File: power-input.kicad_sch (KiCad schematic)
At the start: 21 parts, among them J204 Conn_01x02, J301 Conn_01x02, U202 XL1509-3.3

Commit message: Rename and update layout
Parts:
- removed C201: 22nF, Capacitor_SMD:C_0402_1005Metric, symbol Device:C_Small
- removed D201: B5819W, Diode_SMD:D_SOD-123, symbol Device:D_Schottky
- removed J204: Conn_01x02, Connector_PinHeader_2.54mm:PinHeader_1x02_P2.54mm_Vertical, symbol Connector_Generic:Conn_01x02
- removed J301: Conn_01x02, Connector_Phoenix_MC:PhoenixContact_MCV_1,5_2-G-3.81_1x02_P3.81mm_Vertical, symbol Connector_Generic:Conn_01x02
- removed R211: 0, Resistor_SMD:R_0402_1005Metric, symbol Device:R_Small
- removed R212: inf, Resistor_SMD:R_0402_1005Metric, symbol Device:R_Small
- added C606: 100nF/50V, Capacitor_SMD:C_0402_1005Metric, symbol Device:C
- FB601: renamed from FB301; symbol Device:Ferrite_Bead -> Device:FerriteBead
- renumbered C306 to C601, C302 to C602, C307 to C603, C308 to C604, C301 to C605, C304 to C607, D301 to D601, D303 to D602, D302 to D603, F301 to F601, L302 to L601, L301 to L602, R304 to R601, U202 to U601
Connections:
- net FB is gone; now on net +3V3_1: U601.3 (FB)
- net IN: now also C606.1
- net +3V3 renamed +3V3_1
- net GND renamed GND1
- net GND1: now also C606.2
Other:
- note removed: "CAN wire link"
- note removed: "Prevent feeding Vin to USB"
- title: Sailor Hat with ESP32 -> SH-wg
- moved on the sheet: C601, C603, C604, C605, L601, R601

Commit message: Finish 0.1.0 design
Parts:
- L602: footprint SH-ESP32:SMMS0650-1R0M -> SH-wg:SMMS0650-1R0M
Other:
- title: SH-wg -> Sailor Hat WiFi Gateway
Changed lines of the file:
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@@
   (paper "A4")
   (title_block
-    (title "SH-wg")
+    (title "Sailor Hat WiFi Gateway")
     (date "2022-01-25")
     (rev "0.1.0")
@@
     (effects (font (size 1.27 1.27)) (justify right bottom))
   )
-  (label "FB" (at 241.3 127 0)
-    (effects (font (size 1.27 1.27)) (justify left bottom))
-  )
   (hierarchical_label "Vin" (shape input) (at 49.53 53.34 180)
     (effects (font (size 1.27 1.27)) (justify right))
@@
     (property "Reference" "L602" (id 0) (at 217.17 103.124 90))
     (property "Value" "SMMS0650-470M" (id 1) (at 217.17 105.4354 90))
-    (property "Footprint" "SH-ESP32:SMMS0650-1R0M" (id 2) (at 217.17 107.95 0)
+    (property "Footprint" "SH-wg:SMMS0650-1R0M" (id 2) (at 217.17 107.95 0)
       (effects (font (size 1.27 1.27)) hide)
     )
@@
     (pin "1")
   )
-  (symbol (lib_id "SH-ESP32-mini:+3V3_1") (at 276.86 107.95 0) (unit 1)
+  (symbol (lib_id "SH-wg:+3V3_1") (at 276.86 107.95 0) (unit 1)
     (in_bom yes) (on_board yes) (fields_autoplaced)
     (property "Reference" "#PWR0612" (id 0) (at 276.86 111.76 0)

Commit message: Prepare final 0.1.0 proto
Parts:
- C603: LCSC C28323 -> C215803
- D603: value SS24FL -> B5819W; LCSC C489144 -> C8598
- L601: value NLCV32T-100K-PFR -> CBC3225T100KR; LCSC C74563 -> C90321
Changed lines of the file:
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@@
       (effects (font (size 1.27 1.27)) (justify left))
     )
-    (property "Value" "SS24FL" (id 1) (at 209.0166 112.903 90)
+    (property "Value" "B5819W" (id 1) (at 209.0166 112.903 90)
       (effects (font (size 1.27 1.27)) (justify left))
     )
@@
       (effects (font (size 1.27 1.27)) hide)
     )
-    (property "LCSC" "C489144" (id 5) (at 207.01 111.76 0)
+    (property "LCSC" "C8598" (id 5) (at 207.01 111.76 0)
       (effects (font (size 1.27 1.27)) hide)
     )
@@
     (in_bom yes) (on_board yes)
     (property "Reference" "L601" (id 0) (at 110.49 117.094 90))
-    (property "Value" "NLCV32T-100K-PFR" (id 1) (at 110.49 119.4054 90))
+    (property "Value" "CBC3225T100KR" (id 1) (at 110.49 119.4054 90))
     (property "Footprint" "Inductor_SMD:L_1210_3225Metric" (id 2) (at 110.49 121.92 0)
       (effects (font (size 1.27 1.27)) hide)
@@
       (effects (font (size 1.27 1.27)) hide)
     )
-    (property "LCSC" "C74563" (id 6) (at 110.49 121.92 0)
+    (property "LCSC" "C90321" (id 6) (at 110.49 121.92 0)
       (effects (font (size 1.27 1.27)) hide)
     )
@@
       (effects (font (size 1.27 1.27)) hide)
     )
-    (property "LCSC" "C28323" (id 4) (at 121.92 125.73 0)
-      (effects (font (size 1.27 1.27)) hide)
-    )
+    (property "LCSC" "C215803" (id 4) (at 121.92 125.73 0)
+      (effects (font (size 1.27 1.27)) hide)
+    )

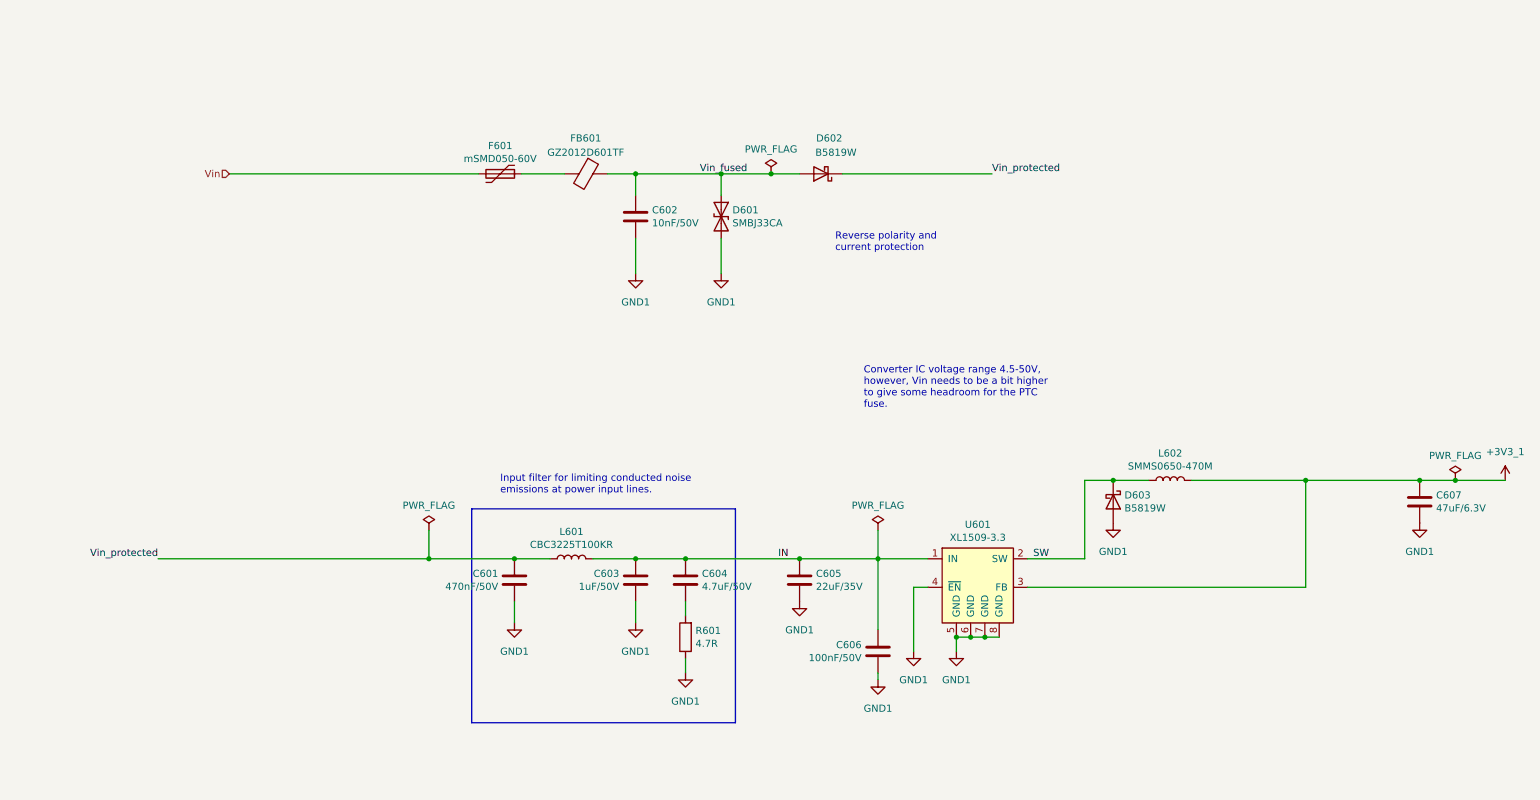
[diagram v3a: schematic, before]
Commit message: Update the design based on the test results
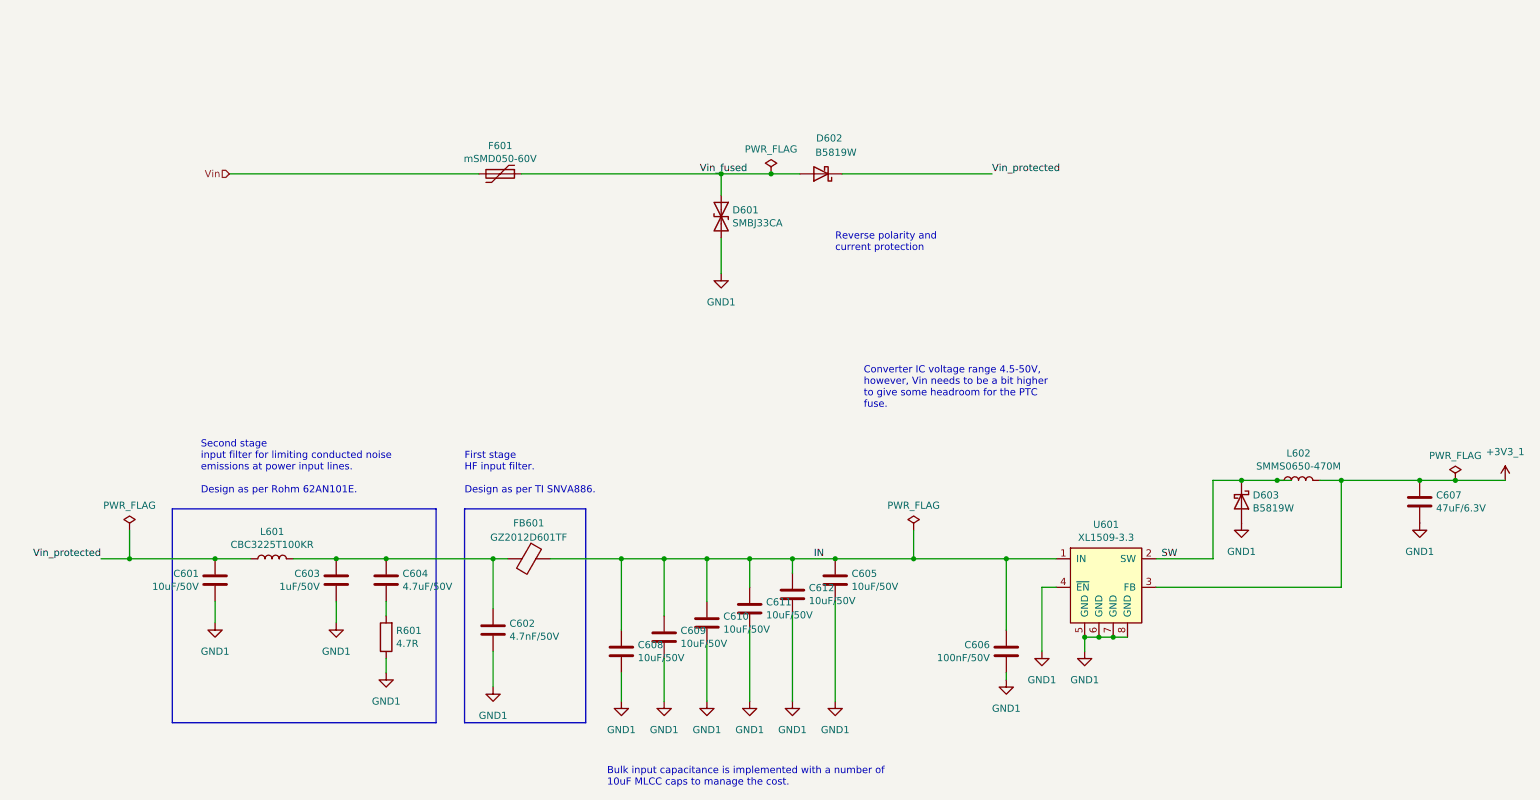
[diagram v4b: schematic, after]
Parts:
- added C608, C609, C610, C611, C612: 10uF/50V, Capacitor_SMD:C_1206_3216Metric, symbol Device:C
- C601: value 470nF/50V -> 10uF/50V; footprint Capacitor_SMD:C_0805_2012Metric -> Capacitor_SMD:C_1206_3216Metric; LCSC C13967 -> C13585
- C602: value 10nF/50V -> 4.7nF/50V; LCSC C15195 -> C1538
- C605: value 22uF/35V -> 10uF/50V; LCSC C342620 -> C13585; Notes 35V -> 50V
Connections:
- net GND1: now also C608.2, C609.2, C610.2, C611.2, C612.2
- net IN: now also FB601.1, C608.1, C609.1, C610.1, C611.1, C612.1; no longer C603.2, C604.1, L601.2
- net Vin_fused: now also F601.1; no longer C602.1, FB601.1
- net at FB601.2: now also C602.1, C603.2, C604.1, L601.2; no longer F601.1
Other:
- note added: "Bulk input capacitance is implemented with a number of 10uF MLCC caps to manage the cost."
- note added: "First stage HF input filter. Design as per TI SNVA886."
- note added: "Second stage input filter for limiting conducted noise emissions at power input lines. Design as per Rohm 62AN101E."
- note removed: "Input filter for limiting conducted noise emissions at power input lines."
- moved on the sheet: C601, C602, C603, C604, C605, C606, D603, FB601, L601, L602, R601, U601

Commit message: Update LED resistor values, improve PCB edge clearance
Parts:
- D602: footprint Diode_SMD:D_SOD-123 -> Diode_SMD:D_SOD-123F
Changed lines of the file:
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@@
       (effects (font (size 1.27 1.27)) (justify left))
     )
-    (property "Footprint" "Diode_SMD:D_SOD-123" (id 2) (at 154.94 53.34 0)
+    (property "Footprint" "Diode_SMD:D_SOD-123F" (id 2) (at 154.94 53.34 0)
       (effects (font (size 1.27 1.27)) hide)
     )
